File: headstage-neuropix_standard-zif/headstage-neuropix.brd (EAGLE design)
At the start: 21.2 x 49.8 mm, 147 parts, among them J1 302-S101, J2 X.FL-R-SMT-1(02), J3 FH23-45S-0.3SHW(05), J5 77311-118-02LF, J6 FH23-45S-0.3SHW(05), U1 10M08SAM15317G, U10 PL133-27GC-R, U11 TS4231, U12 TS4231, U13 TS4231, U2 ASCO2-24.000MHZ-EK-T3, U3 MAX4945AELA+T, U4 DS90UB933_WQFN, U5 NCP161BMX330, U6 TPS8268180, U7 TLV70712, U8 BNO055, U9 DSC6102MI2A-093.6000, X2 OE-LOGO_14X10

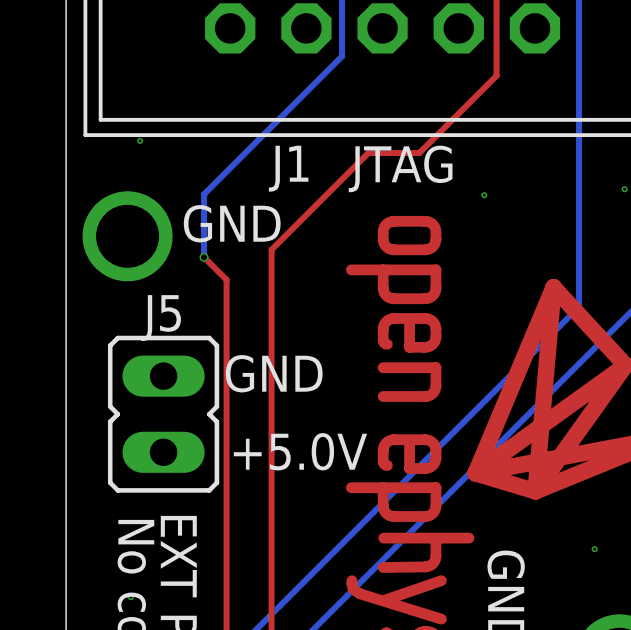
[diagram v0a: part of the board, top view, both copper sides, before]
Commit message: Updated BOM for revision 1.3
- External on google-sheet. Link added to READMEs for each board
version.
- Schematics updated to reflect the BOM.
- Added SMD mount information
- Added .gitignore and .gitattributes for LFS
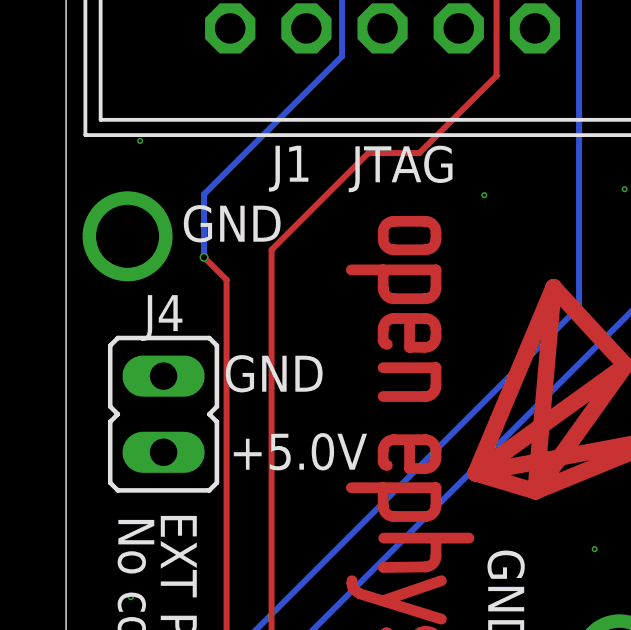
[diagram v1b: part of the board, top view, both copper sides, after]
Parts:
- removed C66: 10uF, jonnew:0402TW
- removed C67: 1uF, jonnew:0201T
- removed J6: FH23-45S-0.3SHW(05), jonnew:1-2013496-8
- added C56: 10nF, jonnew:0201T
- added C60: 1uF, jonnew:0201T
- added J4: 77311-118-02LF, jonnew:JP2
- C24, C26, C28: value 0.1uF -> 10uF; device jonnew:0201T -> jonnew:0402TW
- C25: value 10uF -> 1uF; device jonnew:0402TW -> jonnew:0201T
- C27, C32, C64, C65: value 10uF -> 0.1uF; device jonnew:0402TW -> jonnew:0201T
- C30: value 10nF -> 1nF
- C31, C49: value 10nF -> 0.1uF
- C34, C40, C59: value 0.1uF -> 10nF
- C36, C37: value 10nF -> 10uF; device jonnew:0201T -> jonnew:0402TW
- C38: value 0.1uF -> 1uF
- C41, C42: value 10uF -> 10nF; device jonnew:0402TW -> jonnew:0201T
- C43: value 0.1uF -> 1nF
- C44: value 47nF -> 0.1uF
- C45: value 4.7uF -> 0.1uF; device jonnew:0402T -> jonnew:0201T
- C46: value 10uF -> 0.1uF; device jonnew:0402T -> jonnew:0201T
- C48, C54: value 1uF -> 10uF; device jonnew:0201T -> jonnew:0402TW
- C50: value 0.1uF -> 47nF
- C51: device jonnew:0402T -> jonnew:0402TW
- C52: value 10nF -> 4.7uF; device jonnew:0201T -> jonnew:0402T
- C53: value 1uF -> 10uF; device jonnew:0201T -> jonnew:0402T
- C58: value 0.1uF -> 10uF; device jonnew:0201T -> jonnew:0402T
- C62: value 1nF -> 1uF
- C63: value 1nF -> 0.1uF
- J3: value FH23-45S-0.3SHW(05) -> 1-2013496-8
- J5: value 77311-118-02LF -> 1-2013496-8; device jonnew:JP2 -> jonnew:1-2013496-8
- R21: value 49.9 -> 6.6k
- R23: value 10k -> 49.9
- R24: value 100k -> 10k
- R25: value 2k -> 10k
- R26: value 22 -> 100k
- R27: value 22 -> 2k
- R28: value 20k -> 22
- R29: value 100 -> 20k
- R30: value 15k -> 100
- R31: value 15k -> 22
- R33: value 20k -> 15k
- R34: value 100 -> 15k
- R35: value 6.6k -> 20k
- R36: value 10k -> 100
- U10: value PL133-27GC-R -> BNO055; device jonnew:DFN6_2X1.3_PAD -> jonnew:LGA-28-3.8X5.2
- U11: value TS4231 -> DSC6102MI2A-093.6000; device jonnew:WLCSP3X3 -> jonnew:VFLGA4-2.0X1.6
- U12: value TS4231 -> PL133-27GC-R; device jonnew:WLCSP3X3 -> jonnew:DFN6_2X1.3_PAD
- U14, U15: value (none) -> TS4231; device jonnew:WLCSP6-1X1.2 -> jonnew:WLCSP3X3
- U4: value DS90UB933_WQFN -> ADP7112ACBZ-1.8-R7; device jonnew:WQFN32-5X5 -> jonnew:WLCSP6-1X1.2
- U5: value NCP161BMX330 -> DS90UB933_WQFN; device jonnew:X2SON -> jonnew:WQFN32-5X5
- U6: value TPS8268180 -> NCP161BMX330; device jonnew:MICROSIP9-3X2.3 -> jonnew:X2SON
- U7: value TLV70712 -> TPS8268180; device jonnew:X2SON -> jonnew:MICROSIP9-3X2.3
- U8: value BNO055 -> TLV70712; device jonnew:LGA-28-3.8X5.2 -> jonnew:X2SON
- U9: value DSC6102MI2A-093.6000 -> ADP7112ACBZ-1.2-R7; device jonnew:VFLGA4-2.0X1.6 -> jonnew:WLCSP6-1X1.2
- moved J5 28.4 mm to (0.00, 1.65), flipped to the bottom, turned to 0 degrees
- moved C65 15.9 mm to (7.30, 14.8), flipped to the bottom
- moved C51 15.3 mm to (-7.30, 6.34), turned to 270 degrees
- moved R26 14.9 mm to (-6.15, 14.3), turned to 90 degrees
- moved U15 14.9 mm to (6.60, 13.3), turned to 180 degrees
- moved R35 14.5 mm to (7.20, 5.40)
- moved R36 13.6 mm to (7.20, 4.80), flipped to the bottom
- moved C55 13.0 mm to (-7.37, 14.1), turned to 90 degrees
- moved C62 12.9 mm to (5.45, 11.9), turned to 270 degrees
- moved R32 12.9 mm to (-6.05, 6.40), flipped to the top, turned to 0 degrees
- moved U13 12.9 mm to (-4.60, 7.00), flipped to the top, turned to 0 degrees
- moved C58 12.1 mm to (3.05, 17.6), flipped to the bottom
- moved C48 11.5 mm to (-0.10, 5.12), flipped to the top, turned to 0 degrees
- moved C52 11.4 mm to (-4.02, 13.3), flipped to the bottom
- moved C61 11.1 mm to (-3.10, 7.70), flipped to the top, turned to 180 degrees
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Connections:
- removed net N$9 (its old number): R30.2, U11.B1
- new net N$29: R34.2, U15.B1
- net !IMU_BL: now also R24.2, U10.4; no longer R22.2, U8.4
- net !IMU_RESET: now also R20.1, U10.11; no longer R19.1, U8.11
- net +1V2: now also C48.1, J5.38, J5.39, U8.1; no longer C42.1, J6.38, J6.39, U7.1
- net +1V8: now also C31.1, C34.1, C41.1, C45.1, C53.1, C56.2, C59.2, J5.42, J5.43, R25.1, U11.4, U12.5, U12.6, U5.11, U5.28, U7.A1, U7.A2; no longer C28.1, C30.1, C36.1, C39.1, C46.1, C49.2, C52.2, J6.42, J6.43, R23.1, U10.5, U10.6, U4.11, U4.28, U6.A1, U6.A2, U9.4
- net +3V3: now also C27.1, C32.1, C35.1, C37.1, C47.1, C63.1, C64.1, R20.2, R24.1, U10.28, U10.3, U14.C3, U15.C3, U4.A1, U5.25, U6.1, U8.4, U9.A1; no longer C26.1, C31.1, C33.1, C41.1, C57.1, C58.1, C59.1, R19.2, R20.1, U11.C3, U12.C3, U14.A1, U15.A1, U4.25, U5.1, U7.3, U7.4, U8.28
- net 1V2A: now also C51.1, J5.7, J5.8, U9.A2, U9.B2; no longer C66.1, J6.7, J6.8, U15.A2, U15.B2
- net 1V8A: now also C33.1, J5.3, J5.4, U4.A2, U4.B2; no longer C64.1, J6.3, J6.4, U14.A2, U14.B2
- net BNO_SCL: now also U10.19; no longer U8.19
- net BNO_SDA: now also U10.20; no longer U8.20
- net CAL_A_1KHZ: now also R29.1; no longer R28.1
- net CAL_B_1KHZ: now also R35.1; no longer R33.1
- net CAL_SIGNAL_A: now also R29.2, R30.1; no longer R28.2, R29.1
- net CAL_SIGNAL_A1: now also J5.11, R35.2, R36.1; no longer J6.11, R33.2, R34.1
- net GND: now also C34.2, C39.1, C43.2, C44.2, C52.2, C56.1, C59.1, C60.2, J4.2, J5.1, J5.10, J5.13, J5.14, J5.17, J5.20, J5.23, J5.26, J5.29, J5.32, J5.34, J5.36, J5.37, J5.41, J5.44, J5.45, J5.5, J5.6, J5.9, R19.2, R23.1, R26.2, R30.2, R33.1, R34.1, U10.15, U10.16, U10.17, U10.18, U10.2, U10.25, U10.5, U10.6, U11.2, U12.3, U14.B2, U14.B3, U15.B2, U15.B3, U4.C2, U5.6, U5.7, U6.2, U6.PAD, U7.C1, U7.C2, U7.C3, U8.PAD, U9.C2; no longer C34.1, C39.2, C49.1, C50.2, C52.1, C59.2, C66.2, C67.2, J6.1, J6.10, J6.13, J6.14, J6.17, J6.2, J6.20, J6.23, J6.26, J6.29, J6.32, J6.34, J6.36, J6.37, J6.41, J6.44, J6.45, J6.5, J6.6, J6.9, R21.1, R24.2, R29.2, R30.1, R31.1, R34.2, U10.3, U11.B2, U11.B3, U12.B2, U12.B3, U14.C2, U15.C2, U4.6, U4.7, U4.PAD, U5.2, U6.C1, U6.C2, U6.C3, U7.2, U7.PAD, U8.15, U8.16, U8.17, U8.18, U8.25, U8.5, U8.6, U9.2
- net I2C_SCL_B: now also J5.19; no longer J6.19
- net I2C_SDA_B: now also J5.18; no longer J6.18
- net LH_DATA0: now also U14.C1; no longer U12.C1
- net LH_DATA1: now also U13.C1; no longer U11.C1
- net LH_DATA2: now also U15.C1; no longer U13.C1
- net LH_ENV0: now also U14.C2; no longer U12.C2
- net LH_ENV1: now also U13.C2; no longer U11.C2
- net LH_ENV2: now also U15.C2; no longer U13.C2
- net MIDFILT: now also R27.1; no longer R25.1
- net N$1: now also U11.3, U12.1; no longer U10.1, U9.3
- net N$12: now also C60.1, U13.A1; no longer C53.1, U11.A1
- net N$13: now also C58.1, R27.2; no longer C51.1, R25.2
- net N$14: now also U14.A3; no longer U12.A3
- net N$15: now also U14.A2; no longer U12.A2
- net N$16: now also R33.2, U14.B1; no longer R31.2, U12.B1
- net N$2: now also R28.1, U12.4; no longer R26.1, U10.4
- net N$26: now also U15.A3; no longer U13.A3
- net N$27: now also U15.A2; no longer U13.A2
- net N$28: now also C49.2, U5.13; no longer C43.2, U4.13
- net N$3: now also R31.2; no longer R27.2
- net N$30: now also C55.1, R22.2, U5.9; no longer C48.1, R20.2, U4.9
- net N$31: now also C50.2, U5.12; no longer C44.2, U4.12
- net N$32: now also C50.1, R23.2; no longer C44.1, R21.2
- net N$33: now also C57.1, R25.2, R26.1, U5.8; no longer C50.1, R23.2, R24.1, U4.8
- net N$34: now also C40.1, C44.1, C52.1, U5.10; no longer C35.1, C38.1, C45.1, U4.10
- net N$35: now also C42.1, C46.1, C54.1, U5.14; no longer C37.1, C40.1, C47.1, U4.14
- net N$36: now also C61.1, U14.A1; no longer C54.1, U12.A1
- net N$37: now also C62.1, U15.A1; no longer C55.1, U13.A1
- net N$38: now also C26.1, C28.1, C36.1, U6.3, U6.4, U7.A3, U7.B1, U7.B2, U7.B3; no longer C25.1, C27.1, C32.1, U5.3, U5.4, U6.A3, U6.B1, U6.B2, U6.B3
- net N$39: now also C30.1, U4.B1; no longer C62.1, U14.B1
- net N$40: now also C43.1, U9.B1; no longer C63.1, U15.B1
- net N$41: now also C38.1, R21.1, U9.C1; no longer C67.1, R35.1, U15.C1
- net N$5: now also J5.35, R28.2; no longer J6.35, R26.2
- net N$6: now also R31.1, U12.2; no longer R27.1, U10.2
- net N$67: now also C39.2, U10.9; no longer C34.2, U8.9
- net N$7: now also U13.A3; no longer U11.A3
- net N$8: now also U13.A2; no longer U11.A2
- net NP_OSC_EN: now also U11.1; no longer U9.1
- net NRST: now also J5.15, R21.2, U4.C1; no longer J6.15, R35.2, U14.C1
- net OSC_PDOWN_N_B: now also J5.12; no longer J6.12
- net PSB_CLK_B: now also J5.33; no longer J6.33
- net PSB_DATA_0_B: now also J5.31; no longer J6.31
- net PSB_DATA_1_B: now also J5.30; no longer J6.30
- net PSB_DATA_2_B: now also J5.28; no longer J6.28
- net PSB_DATA_3_B: now also J5.27; no longer J6.27
- net PSB_DATA_4_B: now also J5.25; no longer J6.25
- net PSB_DATA_5_B: now also J5.24; no longer J6.24
- net PSB_DATA_6_B: now also J5.22; no longer J6.22
- net PSB_SYNC_B: now also J5.21; no longer J6.21
- net REC_NRST_B: now also J5.16; no longer J6.16
- net SER_DIN0: now also U5.19; no longer U4.19
- net SER_DIN1: now also U5.20; no longer U4.20
- net SER_DIN10: now also U5.31; no longer U4.31
- net SER_DIN11: now also U5.32; no longer U4.32
- net SER_DIN2: now also U5.21; no longer U4.21
- net SER_DIN3: now also U5.22; no longer U4.22
- net SER_DIN4: now also U5.23; no longer U4.23
- net SER_DIN5: now also U5.24; no longer U4.24
- net SER_DIN6: now also U5.26; no longer U4.26
- net SER_DIN7: now also U5.27; no longer U4.27
- net SER_DIN8: now also U5.29; no longer U4.29
- net SER_DIN9: now also U5.30; no longer U4.30
- net SER_GPIO0: now also U5.15; no longer U4.15
- net SER_GPIO1: now also U5.16; no longer U4.16
- net SER_GPIO2: now also R19.1, U5.17; no longer R36.1, U4.17
- net SER_GPIO3: now also U5.18; no longer U4.18
- net SER_HSYNC: now also U5.1; no longer U4.1
- net SER_PCLK: now also U5.3; no longer U4.3
- net SER_SCL: now also U5.4; no longer U4.4
- net SER_SDA: now also U5.5; no longer U4.5
- net SER_VSYNC: now also U5.2; no longer U4.2
- net SIGOUT: now also C49.1; no longer C43.1
- net VCOAX: now also C25.1, J4.1; no longer C61.1, J5.1
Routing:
- net N$29: track 0.00 -> 0.90 mm
- net N$9 (its old number): track 0.90 -> 0.00 mm

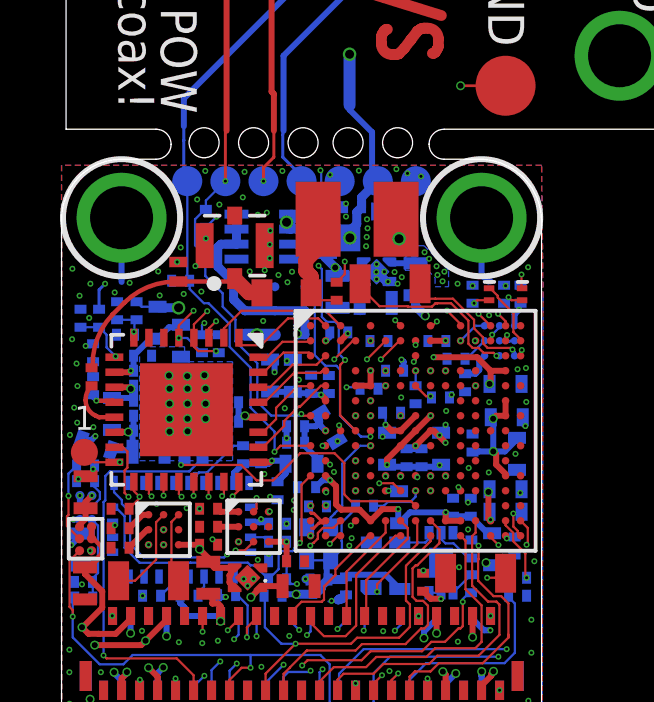
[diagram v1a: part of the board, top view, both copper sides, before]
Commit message: Moved X.FL coax connector up 0.5 mm following OEPS feedback
- Allows more tolerance for passives under it
- Did this for both headstage variants
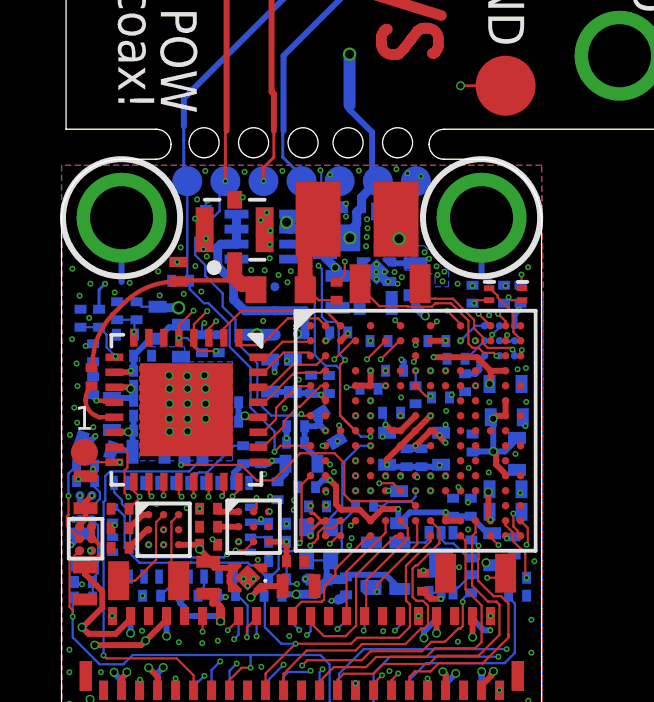
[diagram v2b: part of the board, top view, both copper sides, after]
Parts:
- moved J2 0.53 mm to (-2.23, 17.0)
- moved L10 0.22 mm to (-0.70, 15.0)
- turned R8 to 270 degrees
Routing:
- net GND: vias 171 -> 173
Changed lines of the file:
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@@
 <setting verticaltext="up"/>
 </settings>
-<grid distance="0.1" unitdist="mm" unit="mm" style="lines" multiple="1" display="yes" altdistance="5" altunitdist="mil" altunit="mil"/>
+<grid distance="0.01" unitdist="mm" unit="mm" style="lines" multiple="1" display="yes" altdistance="5" altunitdist="mil" altunit="mil"/>
 <layers>
 <layer number="1" name="Highspeed1" color="4" fill="1" visible="yes" active="yes"/>
@@
 <layer number="27" name="tValues" color="7" fill="1" visible="yes" active="yes"/>
 <layer number="28" name="bValues" color="7" fill="1" visible="yes" active="yes"/>
-<layer number="29" name="tStop" color="7" fill="3" visible="no" active="yes"/>
-<layer number="30" name="bStop" color="7" fill="6" visible="no" active="yes"/>
+<layer number="29" name="tStop" color="7" fill="3" visible="yes" active="yes"/>
+<layer number="30" name="bStop" color="7" fill="6" visible="yes" active="yes"/>
 <layer number="31" name="tCream" color="7" fill="4" visible="no" active="yes"/>
 <layer number="32" name="bCream" color="7" fill="5" visible="no" active="yes"/>
@@
 <element name="U8" library="jonnew" package="X2SON" value="TLV70712" x="-1.8" y="5.4" smashed="yes" rot="R180"/>
 <element name="U5" library="jonnew" package="WQFN32-5X5" value="DS90UB933_WQFN" x="-3.84" y="11" smashed="yes"/>
-<element name="J2" library="jonnew" package="X_FL_R_SMT_1(02)" value="X.FL-R-SMT-1(02)" x="-2.23" y="16.47" smashed="yes"/>
+<element name="J2" library="jonnew" package="X_FL_R_SMT_1(02)" value="X.FL-R-SMT-1(02)" x="-2.23" y="17" smashed="yes"/>
 <element name="D3" library="jonnew" package="0402T-DFN" value="SESD0402X1UN-0020-090" x="-4.11" y="15.6" smashed="yes" rot="R270"/>
 <element name="U1" library="jonnew" package="MBGA153-8X8" value="10M08SAM15317G" x="3.8" y="10.3" smashed="yes"/>
@@
 </element>
 <element name="R5" library="jonnew" package="0201T" value="10k" x="3" y="10.9" smashed="yes" rot="MR180"/>
-<element name="R8" library="jonnew" package="0201T" value="10k" x="-3.19" y="17.38" smashed="yes" rot="MR90"/>
+<element name="R8" library="jonnew" package="0201T" value="10k" x="-3.19" y="17.38" smashed="yes" rot="MR270"/>
 <element name="R13" library="jonnew" package="0201T" value="10k" x="0.68" y="17.83" smashed="yes" rot="MR0"/>
 <element name="R9" library="jonnew" package="0201T" value="1k" x="-4.03" y="15.3" smashed="yes" rot="MR0"/>
@@
 <attribute name="PARTNO" value="C0603X5R1C104K030BC" x="-6.2" y="8.85" size="1.778" layer="28" rot="MR90" display="off"/>
 </element>
-<element name="L10" library="jonnew" package="0603T" value="MPZ1608S102ATA00" x="-0.5" y="14.9" smashed="yes"/>
+<element name="L10" library="jonnew" package="0603T" value="MPZ1608S102ATA00" x="-0.7" y="15" smashed="yes"/>
 <element name="R29" library="jonnew" package="0201T" value="20k" x="-3.9" y="9.6" smashed="yes" rot="MR90"/>
 <element name="R36" library="jonnew" package="0201T" value="100" x="7.2" y="4.8" smashed="yes" rot="MR180"/>
@@
 <via x="2.15" y="16.45" extent="1-16" drill="0.1"/>
 <via x="-7.04" y="15.2" extent="1-16" drill="0.1"/>
-<via x="-0.32" y="15.6" extent="1-16" drill="0.1"/>
+<via x="-0.36" y="15.62" extent="1-16" drill="0.1"/>
 <via x="3.2" y="15.2" extent="1-16" drill="0.1"/>
 <via x="2.5" y="15.35" extent="1-16" drill="0.1"/>
@@
 <via x="7.55" y="15.75" extent="1-16" drill="0.1"/>
 <via x="7.2" y="12.35" extent="1-16" drill="0.1"/>
-<via x="-2.74" y="17.84" extent="1-16" drill="0.1"/>
+<via x="-3.55" y="17.37" extent="1-16" drill="0.1"/>
 <via x="-1.28" y="13.96" extent="1-16" drill="0.1"/>
 <wire x1="-7.197859375" y1="13.125871875" x2="-7.024128125" y2="13.125871875" width="0.15" layer="16"/>
@@
 <wire x1="2.8" y1="8.3" x2="2.9" y2="8.3" width="0.1" layer="1"/>
 <contactref element="U3" pad="5"/>
-<via x="-1.46" y="17.5" extent="1-16" drill="0.1"/>
+<via x="-1.36" y="17.32" extent="1-16" drill="0.1"/>
 <via x="-0.77" y="15.49" extent="1-16" drill="0.1"/>
 <via x="-1.16" y="17.57" extent="1-16" drill="0.1"/>
 <via x="-3.19" y="16.71" extent="1-16" drill="0.1"/>
 <via x="-1.23" y="15.65" extent="1-16" drill="0.1"/>
-<via x="-1.73" y="15.61" extent="1-16" drill="0.1"/>
+<via x="-1.68" y="15.66" extent="1-16" drill="0.1"/>
 <via x="-0.09" y="12" extent="1-16" drill="0.1"/>
 <via x="-0.64" y="18.96" extent="1-16" drill="0.1"/>
@@
 <via x="6.14" y="0.97" extent="1-16" drill="0.1"/>
 <contactref element="R19" pad="2"/>
+<via x="-3.27" y="16.35" extent="1-16" drill="0.1"/>
+<via x="-3.16" y="16.11" extent="1-16" drill="0.1"/>
 </signal>
 <signal name="+3V3">
@@
 <wire x1="-0.9004625" y1="12.2504625" x2="-0.9004625" y2="12.5238625" width="0.2" layer="16"/>
 <wire x1="-0.9004625" y1="12.5238625" x2="-1.05" y2="12.6734" width="0.2" layer="16"/>
-<wire x1="-3.19" y1="17.08" x2="-3.18968125" y2="17.08" width="0.0762" layer="16"/>
-<wire x1="-3.18968125" y1="17.08" x2="-2.834840625" y2="17.434840625" width="0.0762" layer="16"/>
-<via x="-2.834840625" y="17.434840625" extent="1-16" drill="0.1"/>
+<via x="-3.134840625" y="17.974840625" extent="1-16" drill="0.1"/>
 <via x="4.53" y="15.4932" extent="1-16" drill="0.1"/>
 <wire x1="1.27" y1="18.56" x2="1.27" y2="18.62" width="0.0762" layer="16"/>
@@
 <contactref element="C24" pad="1"/>
 <contactref element="U9" pad="A1"/>
-<wire x1="-7.2" y1="7.725" x2="-7.2" y2="7.7166" width="0.2" layer="1"/>
-<wire x1="-7.2" y1="7.725" x2="-7.2" y2="7.93" width="0.2" layer="1"/>
+<wire x1="-7.2" y1="7.7166" x2="-7.2" y2="7.93" width="0.2" layer="1"/>
 <wire x1="-6.99" y1="8.14" x2="-7.2" y2="7.93" width="0.2" layer="1"/>
 <via x="-6.99" y="8.14" extent="1-16" drill="0.1"/>
 <wire x1="-5.3" y1="4.8" x2="-5.3" y2="5.0857" width="0.0762" layer="5"/>
-<wire x1="-7.2" y1="7.725" x2="-7.2" y2="7.3647125" width="0.2" layer="1"/>
+<wire x1="-7.2" y1="7.7166" x2="-7.2" y2="7.3647125" width="0.2" layer="1"/>
 <wire x1="-7.4" y1="7.1647125" x2="-7.4" y2="7.1" width="0.2" layer="1"/>
 <wire x1="-7.2" y1="7.3647125" x2="-7.4" y2="7.1647125" width="0.2" layer="1"/>
+<wire x1="-3.19" y1="17.68" x2="-3.19" y2="17.91968125" width="0.0762" layer="16"/>
+<wire x1="-3.19" y1="17.91968125" x2="-3.134840625" y2="17.974840625" width="0.0762" layer="16"/>
 </signal>
 <signal name="VCOAX">
@@
 <wire x1="-4.105" y1="15.275" x2="-4.1" y2="15.27" width="0.2032" layer="1"/>
 <contactref element="L10" pad="1"/>
-<wire x1="-4.11" y1="15.275" x2="-2.325" y2="15.275" width="0.15" layer="1"/>
-<wire x1="-2.325" y1="15.275" x2="-2.23" y2="15.37" width="0.15" layer="1"/>
-<wire x1="-2.23" y1="15.37" x2="-1.76" y2="14.9" width="0.5" layer="1"/>
-<wire x1="-1.76" y1="14.9" x2="-1.32" y2="14.9" width="0.5" layer="1"/>
+<wire x1="-1.52" y1="15" x2="-1.703" y2="15.183" width="0.5" layer="1"/>
+<wire x1="-2.23" y1="15.9" x2="-2.23" y2="15.41" width="0.5" layer="1"/>
+<wire x1="-2.23" y1="15.41" x2="-2.003" y2="15.183" width="0.5" layer="1"/>
+<wire x1="-2.003" y1="15.183" x2="-1.703" y2="15.183" width="0.5" layer="1"/>
+<wire x1="-2.23" y1="15.41" x2="-2.33" y2="15.31" width="0.15" layer="1"/>
+<wire x1="-2.33" y1="15.31" x2="-3.97" y2="15.31" width="0.15" layer="1"/>
+<wire x1="-3.97" y1="15.31" x2="-4.01" y2="15.27" width="0.15" layer="1"/>
+<wire x1="-4.01" y1="15.27" x2="-4.1" y2="15.27" width="0.15" layer="1"/>
 </signal>
 <signal name="SER_DIN10">
@@
 <wire x1="0.3" y1="10.8" x2="0.05" y2="10.8" width="0.0762" layer="1"/>
 <wire x1="0.05" y1="10.8" x2="-0.01" y2="10.86" width="0.0762" layer="1"/>
-<wire x1="-3.19" y1="17.68" x2="-3.22" y2="17.68" width="0.0762" layer="16"/>
-<wire x1="-3.55" y1="16.48" x2="-3.55" y2="17.35" width="0.0762" layer="16"/>
-<wire x1="-3.22" y1="17.68" x2="-3.55" y2="17.35" width="0.0762" layer="16"/>
-<wire x1="-2.54" y1="18.62" x2="-3.19" y2="17.97" width="0.0762" layer="16"/>
-<wire x1="-3.19" y1="17.97" x2="-3.19" y2="17.68" width="0.0762" layer="16"/>
 <wire x1="-1.475" y1="12.55" x2="-2.2043" y2="13.2793" width="0.0762" layer="16"/>
 <wire x1="-2.2043" y1="14.01" x2="-2.2043" y2="13.2793" width="0.0762" layer="16"/>
@@
 <wire x1="-2.63" y1="14.4357" x2="-2.2043" y2="14.01" width="0.0762" layer="16"/>
 <wire x1="-2.63" y1="14.88" x2="-2.63" y2="14.4357" width="0.0762" layer="16"/>
-<wire x1="-3.21" y1="15.46" x2="-3.21" y2="16.14" width="0.0762" layer="16"/>
-<wire x1="-3.21" y1="16.14" x2="-3.55" y2="16.48" width="0.0762" layer="16"/>
+<wire x1="-3.21" y1="15.82" x2="-3.21" y2="15.46" width="0.0762" layer="16"/>
+<wire x1="-3.55" y1="16.16" x2="-3.21" y2="15.82" width="0.0762" layer="16"/>
+<wire x1="-3.55" y1="16.72" x2="-3.55" y2="16.16" width="0.0762" layer="16"/>
+<wire x1="-3.55" y1="16.72" x2="-3.19" y2="17.08" width="0.0762" layer="16"/>
+<wire x1="-3.19" y1="17.08" x2="-3.19" y2="17.16835625" width="0.0762" layer="16"/>
+<wire x1="-2.735" y1="18.425" x2="-2.54" y2="18.62" width="0.0762" layer="16"/>
+<wire x1="-2.735" y1="17.62335625" x2="-2.735" y2="18.425" width="0.0762" layer="16"/>
+<wire x1="-3.19" y1="17.16835625" x2="-2.735" y2="17.62335625" width="0.0762" layer="16"/>
 </signal>
 <signal name="TCK">
@@
 <wire x1="0.32" y1="16.67" x2="0.55" y2="16.9" width="0.5" layer="1"/>
 <wire x1="1.17" y1="14.65" x2="0.57" y2="14.65" width="0.0762" layer="1"/>
-<wire x1="0.32" y1="14.9" x2="0.57" y2="14.65" width="0.0762" layer="1"/>
-<wire x1="0.14" y1="15.976875" x2="0.14" y2="15.623125" width="0.5" layer="1"/>
-<wire x1="0.55" y1="17.35" x2="0.55" y2="16.386875" width="0.5" layer="1"/>
-<wire x1="0.55" y1="16.386875" x2="0.14" y2="15.976875" width="0.5" layer="1"/>
-<wire x1="0.14" y1="15.623125" x2="0.32" y2="15.443125" width="0.5" layer="1"/>
-<wire x1="0.32" y1="15.443125" x2="0.32" y2="14.9" width="0.5" layer="1"/>
+<wire x1="0.55" y1="17.35" x2="0.12" y2="16.92" width="0.5" layer="1"/>
+<wire x1="0.12" y1="15" x2="0.12" y2="16.92" width="0.5" layer="1"/>
+<wire x1="0.57" y1="14.65" x2="0.22" y2="15" width="0.0762" layer="1"/>
+<wire x1="0.22" y1="15" x2="0.12" y2="15" width="0.0762" layer="1"/>
 </signal>
 <signal name="SER_GPIO0">
